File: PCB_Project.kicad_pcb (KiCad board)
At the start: 8 copper layers, 152.4 x 101.6 mm, 169 parts, among them J1 Picoblade_CFG, J2 DF9-41P-1V32, J3 DF9-CFG-SPW1, Q1 SOC2222AHRG, Q2 SOC2222AHRG, U1 NX1H35 PBGA625, U10 MAX8556ETE, U11 AS4C8M16SA-6TIN, U2 CY15B108QN-40SXI, U3 CY15B108QN-40SXI, U4 CY15B108QN-40SXI, U5 AS4C8M32S-6TIN, U6 M95P32-IXMNT/E, U7 TPS3828-33DBVR, U8 MAX8556ETE, U9 MAX8556ETE, Y2 LFSPXO025225_25MHz

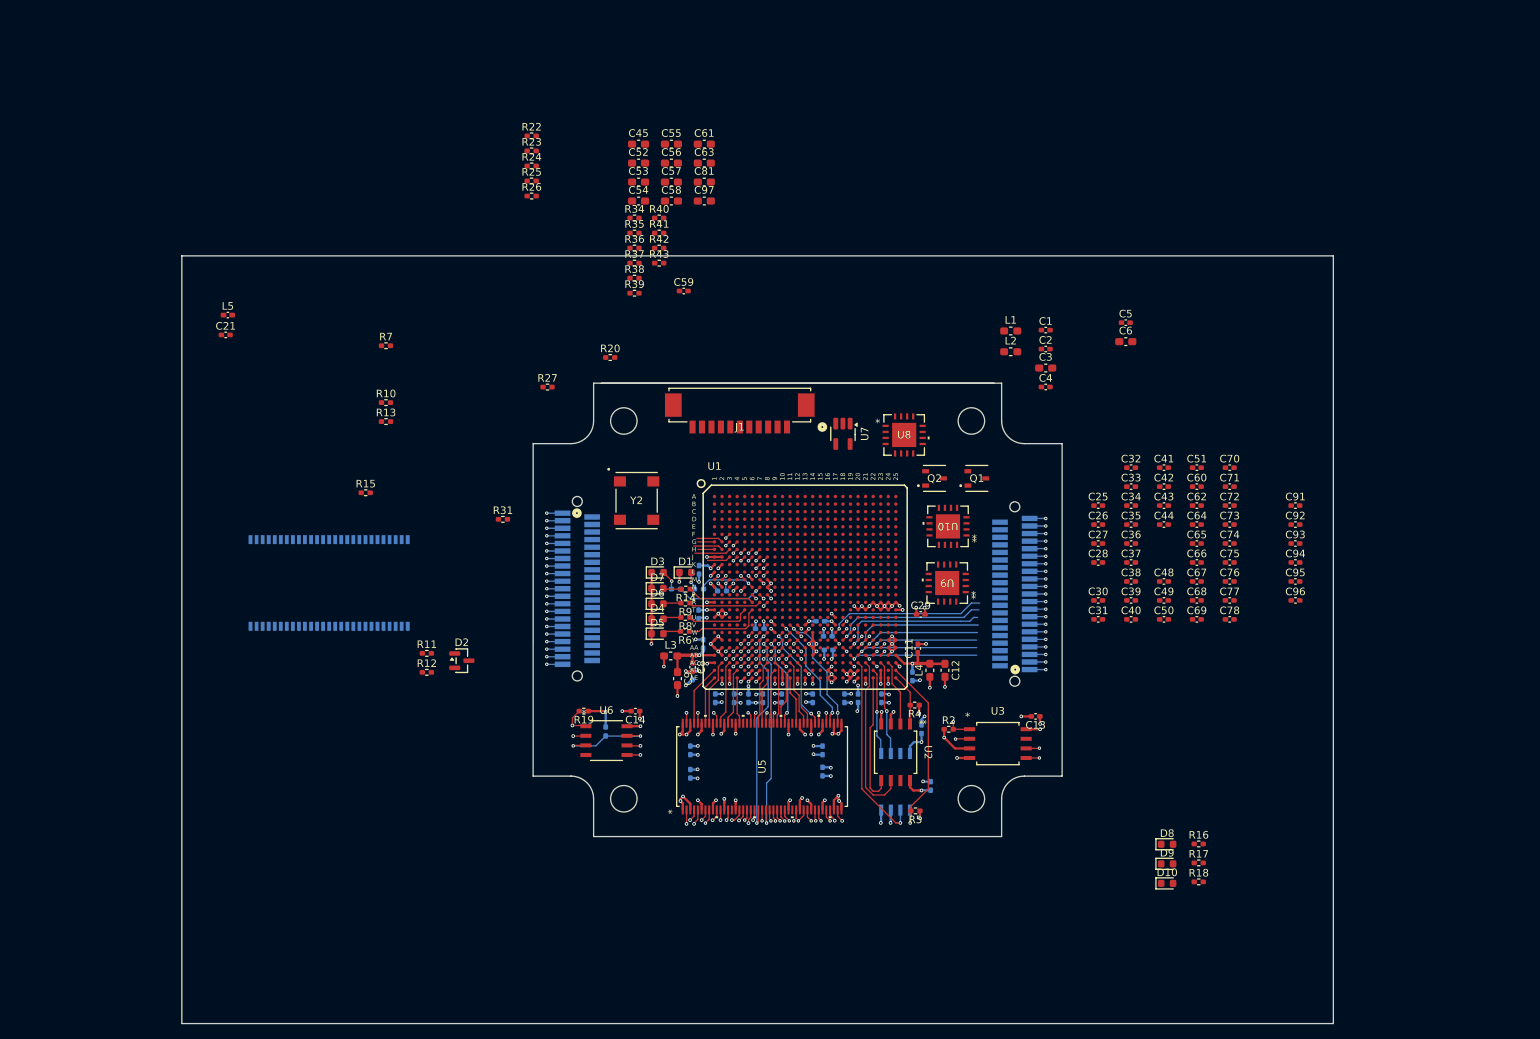
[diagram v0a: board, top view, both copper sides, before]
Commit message: SPW Bank0
completed SPW, rotated edges and adjusted dimensions to make the extra sdram bga fit. completed Bank 0 (still to route to connector). Started fanout of bga sdram
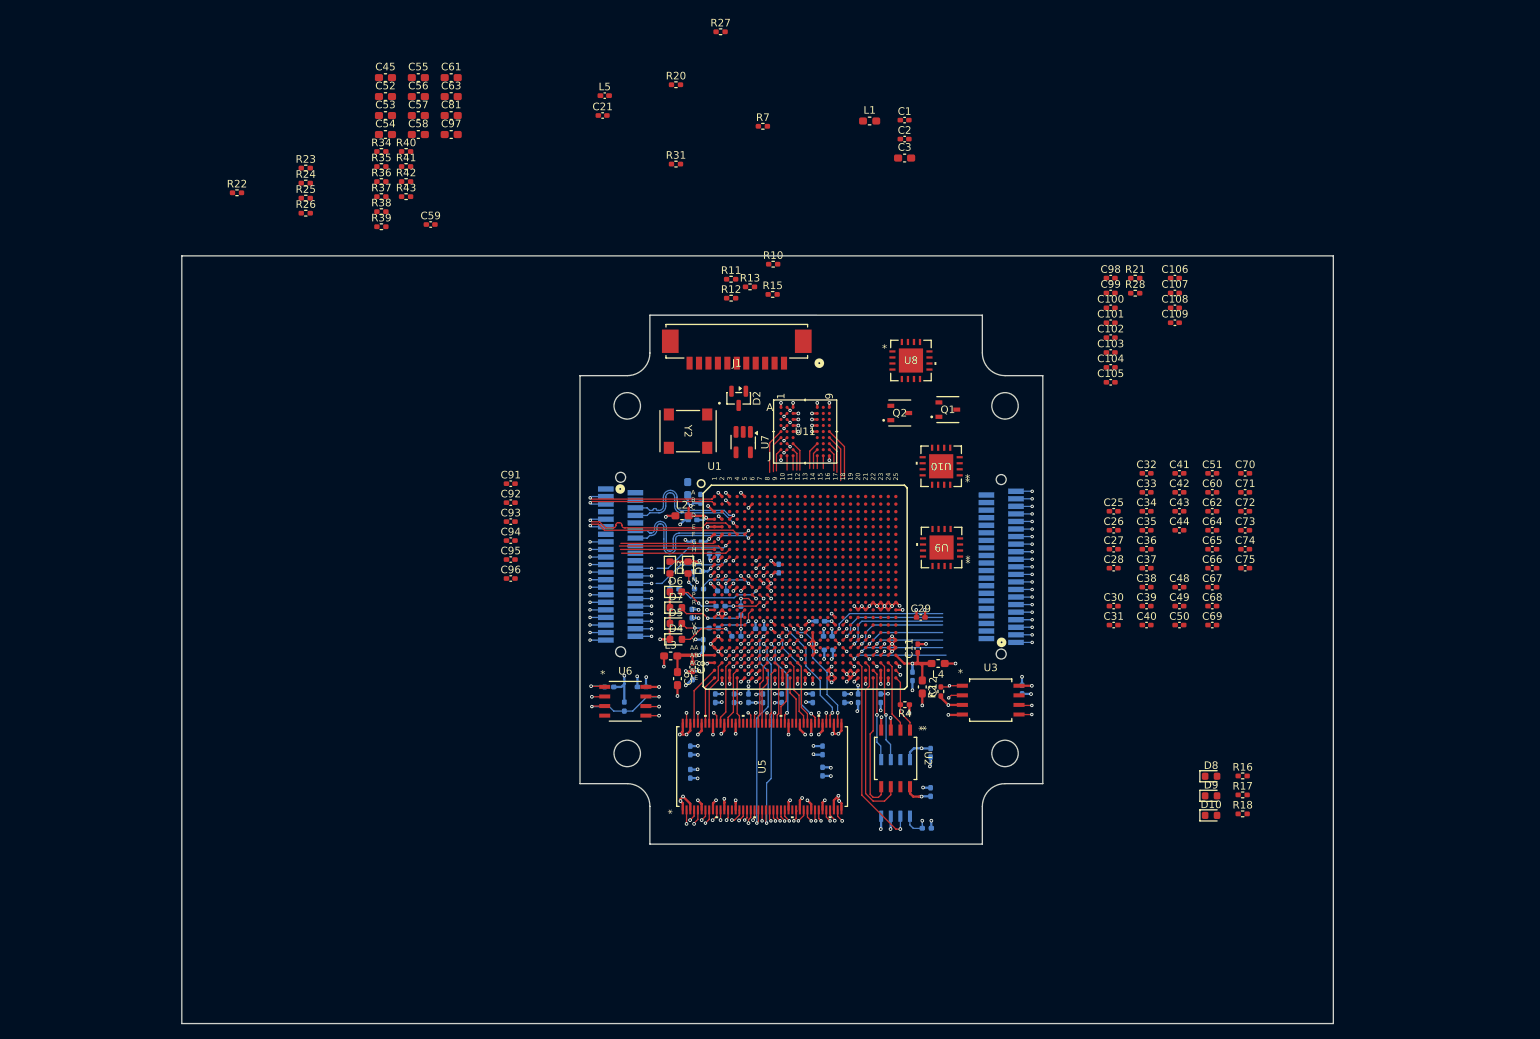
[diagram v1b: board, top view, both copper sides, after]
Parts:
- added C100: 22nF, Capacitor_SMD:C_0402_1005Metric_Pad0.74x0.62mm_HandSolder, F.Cu at (195.2, 61.1)
- added C101: 22nF, Capacitor_SMD:C_0402_1005Metric_Pad0.74x0.62mm_HandSolder, F.Cu at (195.2, 63.1)
- added C102: 100nF, Capacitor_SMD:C_0402_1005Metric_Pad0.74x0.62mm_HandSolder, F.Cu at (195.2, 65.0)
- added C103: 100nF, Capacitor_SMD:C_0402_1005Metric_Pad0.74x0.62mm_HandSolder, F.Cu at (195.2, 67.0)
- added C104: 22nF, Capacitor_SMD:C_0402_1005Metric_Pad0.74x0.62mm_HandSolder, F.Cu at (195.2, 69.0)
- added C105: 22nF, Capacitor_SMD:C_0402_1005Metric_Pad0.74x0.62mm_HandSolder, F.Cu at (195.2, 70.9)
- added C106: 100nF, Capacitor_SMD:C_0402_1005Metric_Pad0.74x0.62mm_HandSolder, F.Cu at (203.7, 57.1)
- added C107: 100nF, Capacitor_SMD:C_0402_1005Metric_Pad0.74x0.62mm_HandSolder, F.Cu at (203.7, 59.1)
- added C108: 100nF, Capacitor_SMD:C_0402_1005Metric_Pad0.74x0.62mm_HandSolder, F.Cu at (203.7, 61.1)
- added C109: 100nF, Capacitor_SMD:C_0402_1005Metric_Pad0.74x0.62mm_HandSolder, F.Cu at (203.7, 63.1)
- added C98: 100nF, Capacitor_SMD:C_0402_1005Metric_Pad0.74x0.62mm_HandSolder, F.Cu at (195.2, 57.1)
- added C99: 100nF, Capacitor_SMD:C_0402_1005Metric_Pad0.74x0.62mm_HandSolder, F.Cu at (195.2, 59.1)
- added R21: 0 Ohm, Resistor_SMD:R_0402_1005Metric_Pad0.72x0.64mm_HandSolder, F.Cu at (198.5, 57.2)
- added R28: 0 Ohm, Resistor_SMD:R_0402_1005Metric_Pad0.72x0.64mm_HandSolder, F.Cu at (198.5, 59.1)
- C13, C14, C4, C5, C6, C76, C77, C78, R14, R19, R5, R6, R8, R9: moved to B.Cu
- U11: value AS4C8M16SA-6TIN -> AS4C8M16S-6BIN; footprint DataHub_Footprints:sdram2_TSOP-54_11P96X22P35_ALL -> DataHub_Footprints:sdram2_bga_TFBGA-54_8X8_ALL; moved to F.Cu
- moved C91 103.9 mm to (115.8, 84.4)
- moved C92 103.9 mm to (115.8, 86.9)
- moved C93 103.9 mm to (115.8, 89.4)
- moved C94 103.9 mm to (115.8, 91.9)
- moved C95 103.9 mm to (115.8, 94.4)
- moved C96 103.9 mm to (115.8, 96.9)
- moved C76 70.7 mm to (140.5, 92.1), turned to 180 degrees
- moved C77 68.6 mm to (142.7, 93.7)
- moved U11 66.1 mm to (154.8, 77.5), turned to 0 degrees
- moved R11 63.8 mm to (145.0, 57.3)
- moved R12 63.8 mm to (145.0, 59.8)
- moved C6 61.2 mm to (139.3, 85.0), turned to 90 degrees
- moved C5 60.9 mm to (141.0, 86.4), turned to 90 degrees
- moved C78 60.1 mm to (151.3, 95.6), turned to 90 degrees
- moved R15 59.9 mm to (150.5, 59.3)
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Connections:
- J3 pad 1: unconnected-(J3-Pad1) -> GND
- J3 pad 10: unconnected-(J3-Pad10) -> GND
- J3 pad 11: unconnected-(J3-Pad11) -> /02_FPGA_Config_JTAG_Bitstream_Reset/SPW1_DOUT_N
- J3 pad 12: unconnected-(J3-Pad12) -> /02_FPGA_Config_JTAG_Bitstream_Reset/SPW1_SOUT_P
- J3 pad 13: unconnected-(J3-Pad13) -> GND
- J3 pad 14: unconnected-(J3-Pad14) -> /02_FPGA_Config_JTAG_Bitstream_Reset/SPW1_SOUT_N
- J3 pad 2: unconnected-(J3-Pad2) -> GND
- J3 pad 29: GND -> unconnected-(J3-Pad29)
- J3 pad 3: unconnected-(J3-Pad3) -> /02_FPGA_Config_JTAG_Bitstream_Reset/SPW1_SIN_P
- J3 pad 30: /02_FPGA_Config_JTAG_Bitstream_Reset/SPW1_DIN_P -> unconnected-(J3-Pad30)
- J3 pad 31: /02_FPGA_Config_JTAG_Bitstream_Reset/SPW1_SOUT_P -> unconnected-(J3-Pad31)
- J3 pad 32: /02_FPGA_Config_JTAG_Bitstream_Reset/SPW1_DIN_N -> unconnected-(J3-Pad32)
- J3 pad 33: /02_FPGA_Config_JTAG_Bitstream_Reset/SPW1_SOUT_N -> unconnected-(J3-Pad33)
- J3 pad 34: GND -> unconnected-(J3-Pad34)
- J3 pad 35: GND -> unconnected-(J3-Pad35)
- J3 pad 36: /02_FPGA_Config_JTAG_Bitstream_Reset/SPW1_SIN_P -> unconnected-(J3-Pad36)
- J3 pad 37: /02_FPGA_Config_JTAG_Bitstream_Reset/SPW1_DOUT_P -> unconnected-(J3-Pad37)
- J3 pad 38: /02_FPGA_Config_JTAG_Bitstream_Reset/SPW1_SIN_N -> unconnected-(J3-Pad38)
- J3 pad 39: /02_FPGA_Config_JTAG_Bitstream_Reset/SPW1_DOUT_N -> unconnected-(J3-Pad39)
- J3 pad 4: unconnected-(J3-Pad4) -> GND
- J3 pad 40: GND -> unconnected-(J3-Pad40)
- J3 pad 41: GND -> unconnected-(J3-Pad41)
- J3 pad 5: unconnected-(J3-Pad5) -> /02_FPGA_Config_JTAG_Bitstream_Reset/SPW1_SIN_N
- J3 pad 6: unconnected-(J3-Pad6) -> /02_FPGA_Config_JTAG_Bitstream_Reset/SPW1_DIN_P
- J3 pad 7: unconnected-(J3-Pad7) -> GND
- J3 pad 8: unconnected-(J3-Pad8) -> /02_FPGA_Config_JTAG_Bitstream_Reset/SPW1_DIN_N
- J3 pad 9: unconnected-(J3-Pad9) -> /02_FPGA_Config_JTAG_Bitstream_Reset/SPW1_DOUT_P
- U1 pad A12: GND -> unconnected-(U1F-VTO_11-PadA12)
- U1 pad A15: GND -> VDDIO_10
- U1 pad A9: GND -> VDDIO_11
- U1 pad B13: GND -> VDDIO_10
- U1 pad B14: GND -> unconnected-(U1B-VTO_10-PadB14)
- U1 pad B18: GND -> unconnected-(U1B-VTO_10-PadB18)
- U1 pad B19: GND -> VDDIO_10
- U1 pad B7: GND -> VDDIO_11
- U1 pad B8: GND -> unconnected-(U1F-VTO_11-PadB8)
- U1 pad D12: GND -> VDDIO_11
- U1 pad F12: GND -> VDDIO_11
- U1 pad H13: GND -> VDDIO_10
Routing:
- net unconnected-(U1A-IO_B0D10N-PadJ8): track 23.7 -> 0.00 mm, vias 1 -> 0
- net unconnected-(U1A-IO_B0D03N-PadJ6): track 23.2 -> 0.00 mm, vias 1 -> 0
- net unconnected-(U1A-IO_B0D02P-PadJ3): track 3.09 -> 24.1 mm, vias 0 -> 1
- net unconnected-(U1A-IO_B0D03P-PadJ5): track 20.3 -> 0.00 mm, vias 1 -> 0
- net /02_FPGA_Config_JTAG_Bitstream_Reset/SPW1_DOUT_N: track 2.15 -> 22.3 mm
- net /02_FPGA_Config_JTAG_Bitstream_Reset/SPW1_DOUT_P: track 2.15 -> 22.2 mm
- net /02_FPGA_Config_JTAG_Bitstream_Reset/SPW1_SOUT_P: track 2.15 -> 22.1 mm
- net /02_FPGA_Config_JTAG_Bitstream_Reset/SPW1_SOUT_N: track 2.15 -> 22.1 mm
- net /02_FPGA_Config_JTAG_Bitstream_Reset/SPW1_SIN_N: track 0.00 -> 19.2 mm, vias 0 -> 1
- net /02_FPGA_Config_JTAG_Bitstream_Reset/SPW1_SIN_P: track 0.00 -> 19.2 mm, vias 0 -> 1
- net /02_FPGA_Config_JTAG_Bitstream_Reset/SPW1_DIN_N: track 0.00 -> 18.3 mm, vias 0 -> 1
- net /02_FPGA_Config_JTAG_Bitstream_Reset/SPW1_DIN_P: track 0.00 -> 18.3 mm, vias 0 -> 1
- net unconnected-(U1D-IO_B5D12N_DQ_SWDO-PadV18): track 24.0 -> 13.0 mm
- net unconnected-(U1D-IO_B5D12P_DQ_SWDO-PadW18): track 24.2 -> 13.2 mm
- net unconnected-(U1D-IO_B5D11N_DQ-PadW19): track 23.0 -> 12.3 mm
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
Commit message: CFG, bga sdram, banks to connectors, docoupling
Finished completely routing bga sdram, finished tracing Banks to connectors DF9. Finished tracing Picoblade, diode, reset supervisor. Finished tracing LEDS on bank 5. Finished decoupling all banks and core. Missing only the power tree and power rail level decoupling.
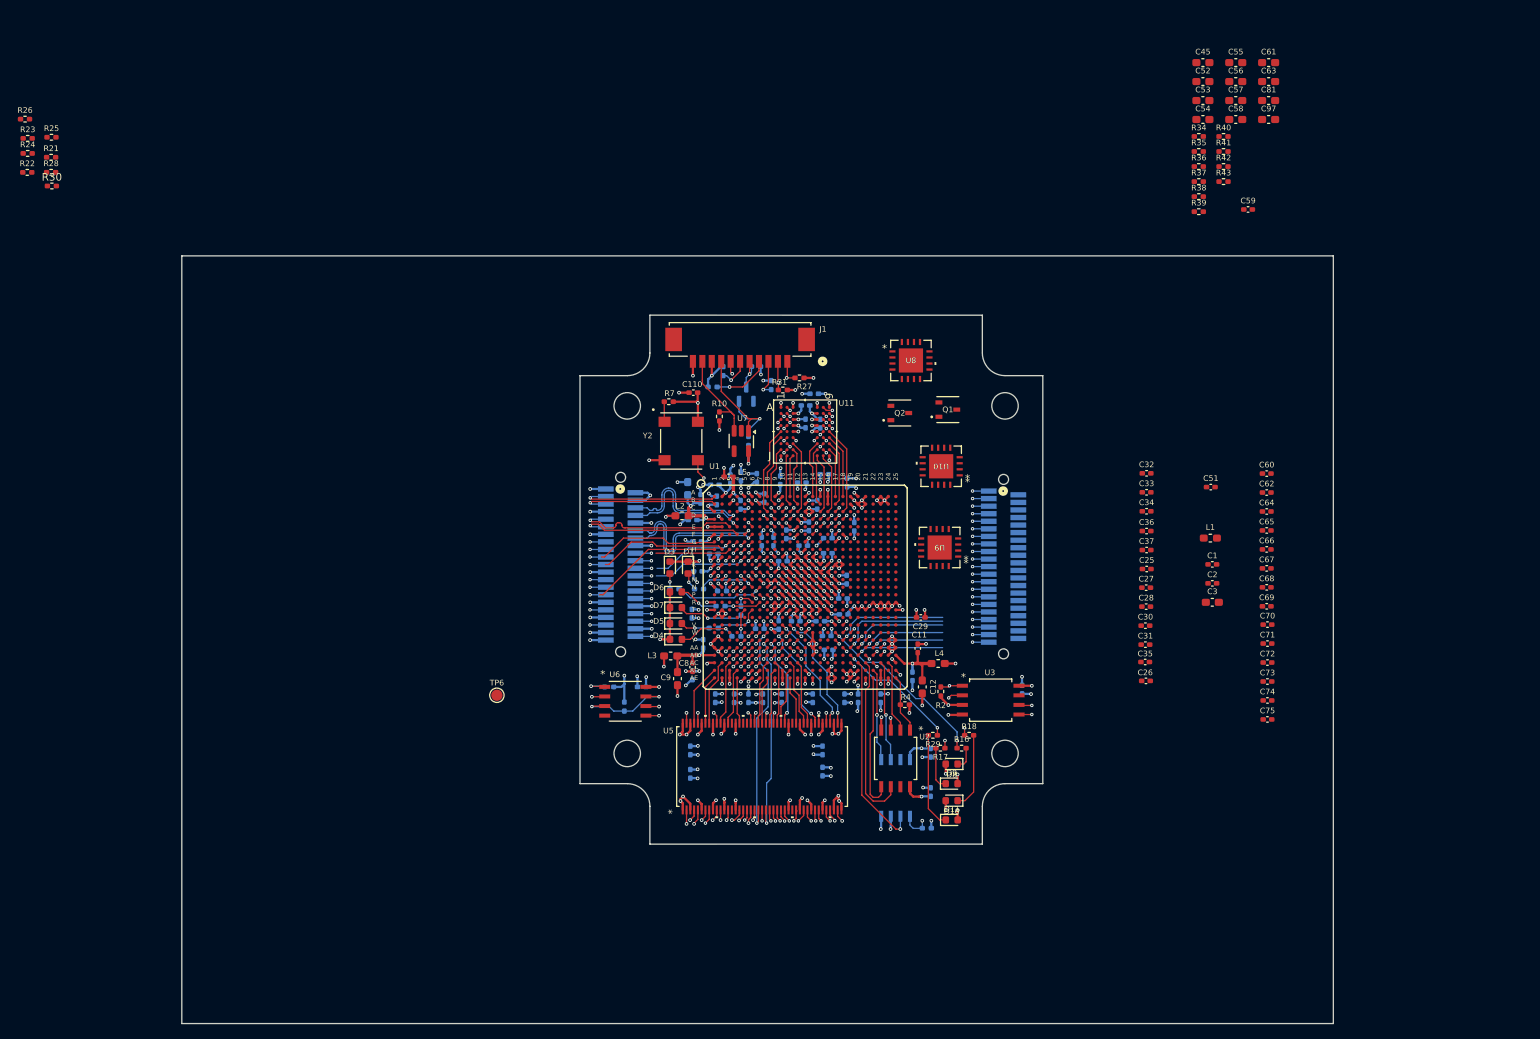
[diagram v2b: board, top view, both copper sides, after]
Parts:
- added C110: 100nF, Capacitor_SMD:C_0402_1005Metric_Pad0.74x0.62mm_HandSolder, F.Cu at (140.0, 72.3)
- added D11: LED_green, LED_SMD:LED_0603_1608Metric, F.Cu at (174.2, 128.9)
- added R29: 1k, Resistor_SMD:R_0402_1005Metric_Pad0.72x0.64mm_HandSolder, F.Cu at (171.7, 117.7)
- added R30: 0 Ohm, Resistor_SMD:R_0402_1005Metric_Pad0.72x0.64mm_HandSolder, F.Cu at (55.1, 45.0)
- added TP6: TestPoint, TestPoint:TestPoint_Pad_D1.5mm, F.Cu at (114.0, 112.4)
- C100, C101, C102, C103, C104, C105, C106, C107, C108, C109, C21, C38, C39, C40, C41, C42, C43, C44, C48, C49, C50, C91, C92, C93, C94, C95, C96, C98, C99, D2, R11, R12, R13, R15, R20: moved to B.Cu
- U11: value AS4C8M16S-6BIN -> AS4C8M16SA-6BIN
- moved R21 144.4 mm to (55.0, 41.2)
- moved R28 144.4 mm to (55.0, 43.1)
- moved C45 108.2 mm to (207.4, 28.6)
- moved C52 108.2 mm to (207.4, 31.1)
- moved C53 108.2 mm to (207.4, 33.6)
- moved C54 108.2 mm to (207.4, 36.2)
- moved C55 108.2 mm to (211.8, 28.6)
- moved C56 108.2 mm to (211.8, 31.1)
- moved C57 108.2 mm to (211.8, 33.6)
- moved C58 108.2 mm to (211.8, 36.2)
- moved C59 108.2 mm to (213.4, 48.1)
- moved C61 108.2 mm to (216.1, 28.6)
- moved C63 108.2 mm to (216.1, 31.1)
- moved C81 108.2 mm to (216.1, 33.6)
- moved C97 108.2 mm to (216.1, 36.2)
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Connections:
- net /02_FPGA_Config_JTAG_Bitstream_Reset/CFG_EEPROM_CLK renamed /02_FPGA_Banks11_12_CFG/CFG_EEPROM_CLK
- net /02_FPGA_Config_JTAG_Bitstream_Reset/CFG_EEPROM_CS_N renamed /02_FPGA_Banks11_12_CFG/CFG_EEPROM_CS_N
- net /02_FPGA_Config_JTAG_Bitstream_Reset/CFG_EEPROM_MISO renamed /02_FPGA_Banks11_12_CFG/CFG_EEPROM_MISO
- net /02_FPGA_Config_JTAG_Bitstream_Reset/CFG_EEPROM_MOSI renamed /02_FPGA_Banks11_12_CFG/CFG_EEPROM_MOSI
- net /02_FPGA_Config_JTAG_Bitstream_Reset/JTCK renamed /02_FPGA_Banks11_12_CFG/JTCK
- net /02_FPGA_Config_JTAG_Bitstream_Reset/JTDI renamed /02_FPGA_Banks11_12_CFG/JTDI
- net /02_FPGA_Config_JTAG_Bitstream_Reset/JTDO renamed /02_FPGA_Banks11_12_CFG/JTDO
- net /02_FPGA_Config_JTAG_Bitstream_Reset/JTMS renamed /02_FPGA_Banks11_12_CFG/JTMS
- net /02_FPGA_Config_JTAG_Bitstream_Reset/JTRST_N renamed /02_FPGA_Banks11_12_CFG/JTRST_N
- net /02_FPGA_Config_JTAG_Bitstream_Reset/LD_CFG0 renamed /02_FPGA_Banks11_12_CFG/LD_CFG0
- net /02_FPGA_Config_JTAG_Bitstream_Reset/LD_CFG1 renamed /02_FPGA_Banks11_12_CFG/LD_CFG1
- net /02_FPGA_Config_JTAG_Bitstream_Reset/LD_CFG2 renamed /02_FPGA_Banks11_12_CFG/LD_CFG2
- net /02_FPGA_Config_JTAG_Bitstream_Reset/LD_CFG3 renamed /02_FPGA_Banks11_12_CFG/LD_CFG3
- net /02_FPGA_Config_JTAG_Bitstream_Reset/MODE0 renamed /02_FPGA_Banks11_12_CFG/MODE0
- net /02_FPGA_Config_JTAG_Bitstream_Reset/MODE1 renamed /02_FPGA_Banks11_12_CFG/MODE1
- net /02_FPGA_Config_JTAG_Bitstream_Reset/OSC0 renamed /02_FPGA_Banks11_12_CFG/OSC0
- net /02_FPGA_Config_JTAG_Bitstream_Reset/PERR renamed /02_FPGA_Banks11_12_CFG/PERR
- net /02_FPGA_Config_JTAG_Bitstream_Reset/PRDY renamed /02_FPGA_Banks11_12_CFG/PRDY
- net /02_FPGA_Config_JTAG_Bitstream_Reset/SPW1_DIN_N renamed /02_FPGA_Banks11_12_CFG/SPW1_DIN_N
- net /02_FPGA_Config_JTAG_Bitstream_Reset/SPW1_DIN_P renamed /02_FPGA_Banks11_12_CFG/SPW1_DIN_P
- net /02_FPGA_Config_JTAG_Bitstream_Reset/SPW1_DOUT_N renamed /02_FPGA_Banks11_12_CFG/SPW1_DOUT_N
- net /02_FPGA_Config_JTAG_Bitstream_Reset/SPW1_DOUT_P renamed /02_FPGA_Banks11_12_CFG/SPW1_DOUT_P
- net /02_FPGA_Config_JTAG_Bitstream_Reset/SPW1_SIN_N renamed /02_FPGA_Banks11_12_CFG/SPW1_SIN_N
- net /02_FPGA_Config_JTAG_Bitstream_Reset/SPW1_SIN_P renamed /02_FPGA_Banks11_12_CFG/SPW1_SIN_P
- net /02_FPGA_Config_JTAG_Bitstream_Reset/SPW1_SOUT_N renamed /02_FPGA_Banks11_12_CFG/SPW1_SOUT_N
- net /02_FPGA_Config_JTAG_Bitstream_Reset/SPW1_SOUT_P renamed /02_FPGA_Banks11_12_CFG/SPW1_SOUT_P
- net VDDSEN renamed CORE_VDDSEN
- C14 pad 1: VDD3V3 -> VDDIO_SERVICE
- C22 pad 1: VDD2V5 -> VDD2V5A
- C23 pad 1: VDD2V5 -> VDD2V5A
- C24 pad 1: VDD2V5 -> VDD2V5A
- C29 pad 1: VDD2V5 -> VDD2V5A
- C46 pad 1: VDD2V5 -> VDD2V5A
- C47 pad 1: VDD2V5 -> VDD2V5A
- C48 pad 1: VDD2V5 -> VDD2V5A
- C49 pad 1: VDD2V5 -> VDD2V5A
- C50 pad 1: VDD2V5 -> VDD2V5A
- C51 pad 1: VDD2V5 -> VDD2V5A
- C53 pad 1: VDD2V5 -> VDD2V5A
- C54 pad 1: VDD2V5 -> VDD2V5A
- J1 pad 9: VDD3V3 -> VDDIO_SERVICE
- J3 pad 16: unconnected-(J3-Pad16) -> GND
- J3 pad 23: unconnected-(J3-Pad23) -> GND
- J3 pad 31: unconnected-(J3-Pad31) -> GND
- J3 pad 32: unconnected-(J3-Pad32) -> GND
- J3 pad 35: unconnected-(J3-Pad35) -> GND
- J3 pad 38: unconnected-(J3-Pad38) -> GND
- J3 pad 39: unconnected-(J3-Pad39) -> GND
- J3 pad 41: unconnected-(J3-Pad41) -> GND
- Q1 pad 3: VDD3V3 -> VDDIO_SERVICE
- R10 pad 1: VDD3V3 -> VDDIO_SERVICE
- R11 pad 1: VDD3V3 -> VDDIO_SERVICE
- R12 pad 1: VDD3V3 -> VDDIO_SERVICE
- R13 pad 1: VDD3V3 -> VDDIO_SERVICE
- R15 pad 1: VDD3V3 -> VDDIO_SERVICE
- R16 pad 1: /03_FPGA_Bank0_Dsu_UART/LD_USER1 -> /05_FPGA_Bank5_SPI/LD_USER1
- R17 pad 1: /03_FPGA_Bank0_Dsu_UART/LD_USER2 -> /05_FPGA_Bank5_SPI/LD_USER2
- R18 pad 1: /03_FPGA_Bank0_Dsu_UART/LD_USER3 -> /05_FPGA_Bank5_SPI/LD_USER3
- R19 pad 1: VDD3V3 -> VDDIO_SERVICE
- R26 pad 2: VDD3V3 -> VDD2V5
- R31 pad 2: VDD3V3 -> VDDIO_SERVICE
- R32 pad 1: VDD3V3 -> VDDIO_SERVICE
- R33 pad 2: VDD3V3 -> VDDIO_SERVICE
- R35 pad 1: VDD2V5 -> VDD2V5A
- R40 pad 1: VDD3V3 -> VDDIO_SERVICE
- U1 pad A11: unconnected-(U1F-IO_B11D09P-PadA11) -> /02_FPGA_Banks11_12_CFG/SDRAM_B_A4
- U1 pad A13: VDD2V5 -> VDD2V5A
- U1 pad A14: unconnected-(U1B-IO_B10D03P_DQS_SWDI-PadA14) -> /07_FPGA_Bank10_SDRAMB/SDRAM_B_BA0
- U1 pad A17: unconnected-(U1B-IO_B10D12N_DQ_SWDO-PadA17) -> /07_FPGA_Bank10_SDRAMB/SDRAM_B_A10
- U1 pad A18: unconnected-(U1B-IO_B10D12P_DQ_SWDO-PadA18) -> /07_FPGA_Bank10_SDRAMB/SDRAM_B_WE_N
- U1 pad A20: VDD2V5 -> VDD2V5A
- U1 pad A6: VDD2V5 -> VDD2V5A
- U1 pad A8: unconnected-(U1F-IO_B11D05P_DQ-PadA8) -> /02_FPGA_Banks11_12_CFG/SDRAM_B_UDQM
- U1 pad AB19: unconnected-(U1D-IO_B5D15N_DQ_SWSI-PadAB19) -> /05_FPGA_Bank5_SPI/LD_USER4
- U1 pad AB21: unconnected-(U1D-IO_B5D07P-PadAB21) -> /05_FPGA_Bank5_SPI/LD_USER2
- U1 pad AB22: unconnected-(U1D-IO_B5D04P_DQ_SWSI-PadAB22) -> /05_FPGA_Bank5_SPI/LD_USER3
- U1 pad AE13: VDD2V5 -> VDD2V5A
- U1 pad AE20: VDD2V5 -> VDD2V5A
- U1 pad AE6: VDD2V5 -> VDD2V5A
- U1 pad B11: unconnected-(U1F-IO_B11D09N-PadB11) -> /02_FPGA_Banks11_12_CFG/SDRAM_B_A5
- U1 pad B12: unconnected-(U1F-IO_B11D13P_DQS_SWSO-PadB12) -> /02_FPGA_Banks11_12_CFG/SDRAM_B_A6
- U1 pad B15: unconnected-(U1B-IO_B10D03N_DQS_SWDI-PadB15) -> /07_FPGA_Bank10_SDRAMB/SDRAM_B_A0
- U1 pad B17: unconnected-(U1B-IO_B10D07P-PadB17) -> /07_FPGA_Bank10_SDRAMB/SDRAM_B_CS_N
- U1 pad B9: unconnected-(U1F-IO_B11D05N_DQ-PadB9) -> /02_FPGA_Banks11_12_CFG/SDRAM_B_A8
- U1 pad C10: unconnected-(U1F-IO_B11D08N-PadC10) -> /02_FPGA_Banks11_12_CFG/SDRAM_B_A7
- U1 pad C11: unconnected-(U1F-IO_B11D08P-PadC11) -> /02_FPGA_Banks11_12_CFG/SDRAM_B_DQ11
- U1 pad C12: unconnected-(U1F-IO_B11D13N_DQS_SWSO-PadC12) -> /02_FPGA_Banks11_12_CFG/SDRAM_B_A9
- U1 pad C15: unconnected-(U1B-IO_B10D02P_DQ_SWSO-PadC15) -> /07_FPGA_Bank10_SDRAMB/SDRAM_B_A3
- U1 pad C16: unconnected-(U1B-IO_B10D04P_DQ_SWSI-PadC16) -> /07_FPGA_Bank10_SDRAMB/SDRAM_B_A2
- U1 pad C17: unconnected-(U1B-IO_B10D07N-PadC17) -> /07_FPGA_Bank10_SDRAMB/SDRAM_B_DQ5
- U1 pad C18: unconnected-(U1B-IO_B10D13P_DQS_SWSO-PadC18) -> /07_FPGA_Bank10_SDRAMB/SDRAM_B_DQ7
- U1 pad C8: unconnected-(U1F-IO_B11D03P_DQS_SWDI-PadC8) -> /02_FPGA_Banks11_12_CFG/SDRAM_B_DQ8
- U1 pad C9: unconnected-(U1F-IO_B11D06P_DQ-PadC9) -> /02_FPGA_Banks11_12_CFG/SDRAM_B_DQ9
- U1 pad D10: unconnected-(U1F-IO_B11D07P-PadD10) -> /02_FPGA_Banks11_12_CFG/SDRAM_B_A11
- U1 pad D11: unconnected-(U1F-IO_B11D10P-PadD11) -> /02_FPGA_Banks11_12_CFG/SDRAM_B_DQ13
- U1 pad D13: unconnected-(U1F-IO_B11D14P_DQ_SWDI-PadD13) -> /02_FPGA_Banks11_12_CFG/SDRAM_B_DQ15
- U1 pad D14: unconnected-(U1B-IO_B10D02N_DQ_SWSO-PadD14) -> /07_FPGA_Bank10_SDRAMB/SDRAM_B_BA1
- U1 pad D15: unconnected-(U1B-IO_B10D04N_DQ_SWSI-PadD15) -> /07_FPGA_Bank10_SDRAMB/SDRAM_B_A1
- U1 pad D16: unconnected-(U1B-IO_B10D08N-PadD16) -> /07_FPGA_Bank10_SDRAMB/SDRAM_B_DQ6
- U1 pad D17: unconnected-(U1B-IO_B10D08P-PadD17) -> /07_FPGA_Bank10_SDRAMB/SDRAM_B_DQ2
- U1 pad D18: unconnected-(U1B-IO_B10D13N_DQS_SWSO-PadD18) -> /07_FPGA_Bank10_SDRAMB/SDRAM_B_DQ1
- U1 pad D8: unconnected-(U1F-IO_B11D03N_DQS_SWDI-PadD8) -> /02_FPGA_Banks11_12_CFG/SDRAM_B_DQ10
- U1 pad D9: unconnected-(U1F-IO_B11D06N_CAL-PadD9) -> /02_FPGA_Banks11_12_CFG/SDRAM_B_CLK
- U1 pad E10: unconnected-(U1F-IO_B11D07N-PadE10) -> /02_FPGA_Banks11_12_CFG/SDRAM_B_DQ14
- U1 pad E11: unconnected-(U1F-IO_B11D10N_DQ-PadE11) -> /02_FPGA_Banks11_12_CFG/SDRAM_B_CKE
- U1 pad E14: unconnected-(U1B-IO_B10D01P_DQ_SWDO-PadE14) -> /07_FPGA_Bank10_SDRAMB/SDRAM_B_CAS_N
- U1 pad E15: unconnected-(U1B-IO_B10D05P_DQ-PadE15) -> /07_FPGA_Bank10_SDRAMB/SDRAM_B_RAS_N
- U1 pad E16: unconnected-(U1B-IO_B10D09P-PadE16) -> /07_FPGA_Bank10_SDRAMB/SDRAM_B_DQ4
- U1 pad E17: unconnected-(U1B-IO_B10D14P_DQ_SWDI-PadE17) -> /07_FPGA_Bank10_SDRAMB/SDRAM_B_DQ3
- U1 pad E9: unconnected-(U1F-IO_B11D04P_DQ_SWSI-PadE9) -> /02_FPGA_Banks11_12_CFG/SDRAM_B_DQ12
- U1 pad F14: unconnected-(U1B-IO_B10D05N_DQ-PadF14) -> /07_FPGA_Bank10_SDRAMB/SDRAM_B_LDQM
- U1 pad F17: unconnected-(U1B-IO_B10D14N_DQ_SWDI-PadF17) -> /07_FPGA_Bank10_SDRAMB/SDRAM_B_DQ0
- U1 pad K1: VDD2V5 -> VDD2V5A
- U1 pad K25: VDD2V5 -> VDD2V5A
- U1 pad M7: VDD3V3 -> VDDIO_SERVICE
- U1 pad N1: VDD3V3 -> VDDIO_SERVICE
- U1 pad N5: VDD3V3 -> VDDIO_SERVICE
- U1 pad R1: VDD3V3 -> VDDIO_SERVICE
- U1 pad T1: VDD2V5 -> VDD2V5A
- U1 pad T25: VDD2V5 -> VDD2V5A
- U1 pad W17: unconnected-(U1D-IO_B5D14N_DQ_SWDI-PadW17) -> /05_FPGA_Bank5_SPI/LD_USER1
- U11 pad A2: unconnected-(U11-DQ15-PadA2) -> /02_FPGA_Banks11_12_CFG/SDRAM_B_DQ15
- U11 pad A8: unconnected-(U11-DQ0-PadA8) -> /07_FPGA_Bank10_SDRAMB/SDRAM_B_DQ0
- U11 pad B1: unconnected-(U11-DQ14-PadB1) -> /02_FPGA_Banks11_12_CFG/SDRAM_B_DQ14
- U11 pad B2: unconnected-(U11-DQ13-PadB2) -> /02_FPGA_Banks11_12_CFG/SDRAM_B_DQ13
- U11 pad B8: unconnected-(U11-DQ2-PadB8) -> /07_FPGA_Bank10_SDRAMB/SDRAM_B_DQ2
- U11 pad B9: unconnected-(U11-DQ1-PadB9) -> /07_FPGA_Bank10_SDRAMB/SDRAM_B_DQ1
- U11 pad C1: unconnected-(U11-DQ12-PadC1) -> /02_FPGA_Banks11_12_CFG/SDRAM_B_DQ12
- U11 pad C2: unconnected-(U11-DQ11-PadC2) -> /02_FPGA_Banks11_12_CFG/SDRAM_B_DQ11
- U11 pad C8: unconnected-(U11-DQ4-PadC8) -> /07_FPGA_Bank10_SDRAMB/SDRAM_B_DQ4
- U11 pad C9: unconnected-(U11-DQ3-PadC9) -> /07_FPGA_Bank10_SDRAMB/SDRAM_B_DQ3
- U11 pad D1: unconnected-(U11-DQ10-PadD1) -> /02_FPGA_Banks11_12_CFG/SDRAM_B_DQ10
- U11 pad D2: unconnected-(U11-DQ9-PadD2) -> /02_FPGA_Banks11_12_CFG/SDRAM_B_DQ9
- U11 pad D8: unconnected-(U11-DQ6-PadD8) -> /07_FPGA_Bank10_SDRAMB/SDRAM_B_DQ6
- U11 pad D9: unconnected-(U11-DQ5-PadD9) -> /07_FPGA_Bank10_SDRAMB/SDRAM_B_DQ5
- U11 pad E1: unconnected-(U11-DQ8-PadE1) -> /02_FPGA_Banks11_12_CFG/SDRAM_B_DQ8
- U11 pad E8: unconnected-(U11-LDQM-PadE8) -> /07_FPGA_Bank10_SDRAMB/SDRAM_B_LDQM
- U11 pad E9: unconnected-(U11-DQ7-PadE9) -> /07_FPGA_Bank10_SDRAMB/SDRAM_B_DQ7
- U11 pad F1: unconnected-(U11-UDQM-PadF1) -> /02_FPGA_Banks11_12_CFG/SDRAM_B_UDQM
- U11 pad F2: /07_IO_DF9_connectors/SDRAM_B_CLK -> /02_FPGA_Banks11_12_CFG/SDRAM_B_CLK
- U11 pad F3: /07_IO_DF9_connectors/SDRAM_B_CKE -> /02_FPGA_Banks11_12_CFG/SDRAM_B_CKE
- U11 pad F7: unconnected-(U11-*CAS-PadF7) -> /07_FPGA_Bank10_SDRAMB/SDRAM_B_CAS_N
- U11 pad F8: unconnected-(U11-*RAS-PadF8) -> /07_FPGA_Bank10_SDRAMB/SDRAM_B_RAS_N
- U11 pad F9: unconnected-(U11-*WE-PadF9) -> /07_FPGA_Bank10_SDRAMB/SDRAM_B_WE_N
- U11 pad G2: unconnected-(U11-A11-PadG2) -> /02_FPGA_Banks11_12_CFG/SDRAM_B_A11
- U11 pad G3: unconnected-(U11-A9-PadG3) -> /02_FPGA_Banks11_12_CFG/SDRAM_B_A9
- U11 pad G7: unconnected-(U11-BA0-PadG7) -> /07_FPGA_Bank10_SDRAMB/SDRAM_B_BA0
- U11 pad G8: unconnected-(U11-BA1-PadG8) -> /07_FPGA_Bank10_SDRAMB/SDRAM_B_BA1
- U11 pad G9: unconnected-(U11-*CS-PadG9) -> /07_FPGA_Bank10_SDRAMB/SDRAM_B_CS_N
- U11 pad H1: unconnected-(U11-A8-PadH1) -> /02_FPGA_Banks11_12_CFG/SDRAM_B_A8
- U11 pad H2: unconnected-(U11-A7-PadH2) -> /02_FPGA_Banks11_12_CFG/SDRAM_B_A7
- U11 pad H3: unconnected-(U11-A6-PadH3) -> /02_FPGA_Banks11_12_CFG/SDRAM_B_A6
- U11 pad H7: unconnected-(U11-A0-PadH7) -> /07_FPGA_Bank10_SDRAMB/SDRAM_B_A0
- U11 pad H8: unconnected-(U11-A1-PadH8) -> /07_FPGA_Bank10_SDRAMB/SDRAM_B_A1
- U11 pad H9: unconnected-(U11-A10-PadH9) -> /07_FPGA_Bank10_SDRAMB/SDRAM_B_A10
- U11 pad J2: unconnected-(U11-A5-PadJ2) -> /02_FPGA_Banks11_12_CFG/SDRAM_B_A5
- U11 pad J3: unconnected-(U11-A4-PadJ3) -> /02_FPGA_Banks11_12_CFG/SDRAM_B_A4
- U11 pad J7: unconnected-(U11-A3-PadJ7) -> /07_FPGA_Bank10_SDRAMB/SDRAM_B_A3
- U11 pad J8: unconnected-(U11-A2-PadJ8) -> /07_FPGA_Bank10_SDRAMB/SDRAM_B_A2
- U6 pad 8: VDD3V3 -> VDDIO_SERVICE
- U7 pad 5: VDD3V3 -> VDDIO_SERVICE
- U9 pad 10: VDD2V5 -> VDD2V5A
- U9 pad 11: VDD2V5 -> VDD2V5A
- U9 pad 7: VDD2V5 -> VDD2V5A
- U9 pad 8: VDD2V5 -> VDD2V5A
- U9 pad 9: VDD2V5 -> VDD2V5A
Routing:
- net GND: track 143.5 -> 285.6 mm, vias 103 -> 196
- net VDD1V2: track 4.17 -> 51.4 mm, vias 3 -> 37
- net RST_N: track 0.00 -> 41.6 mm, vias 0 -> 2
- net /02_FPGA_Banks11_12_CFG/JTRST_N: track 0.00 -> 32.7 mm, vias 0 -> 2
- net VDDIO_SERVICE: track 0.00 -> 25.7 mm, vias 0 -> 12
- net unconnected-(U1A-IO_B0D07N-PadH6): track 0.00 -> 24.0 mm, vias 0 -> 1
- net /05_FPGA_Bank5_SPI/LD_USER1: track 0.00 -> 23.7 mm, vias 0 -> 2
- net unconnected-(U1A-IO_B0D11P_CLK1-PadG6): track 0.00 -> 22.2 mm, vias 0 -> 1
- net unconnected-(U1A-IO_B0D09N-PadG5): track 0.00 -> 21.3 mm, vias 0 -> 1
- net unconnected-(U1A-IO_B0D09P-PadG4): track 0.00 -> 20.6 mm, vias 0 -> 1
- net unconnected-(U1A-IO_B0D06N-PadH4): track 0.00 -> 20.3 mm, vias 0 -> 1
- net /07_FPGA_Bank10_SDRAMB/SDRAM_B_DQ0: track 0.00 -> 19.5 mm, vias 0 -> 2
- net /02_FPGA_Banks11_12_CFG/JTDI: track 13.4 -> 32.7 mm, vias 1 -> 2
- net /02_FPGA_Banks11_12_CFG/JTMS: track 14.4 -> 33.6 mm, vias 1 -> 2
- net /05_FPGA_Bank5_SPI/LD_USER3: track 0.00 -> 18.8 mm, vias 0 -> 2
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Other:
- board text added: "9"
- board text added: "A"
- board text added: "J"
